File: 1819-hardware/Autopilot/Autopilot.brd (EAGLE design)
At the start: 44.8 x 54 mm, 36 parts, among them U1 MAX3485CSA, U3 PCA9306, U4 74HC1G04

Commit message: updated Autopilot board files
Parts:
- removed B2: Pressure Sensor, SparkFun-Boards:SPARKFUN_MS5803-14BA_BREAKOUT
- added J6: (no value), SparkFun-Connectors:1X07_NO_SILK
- moved R14 35.6 mm to (34.3, 22.2), flipped to the bottom
- moved C5 31.6 mm to (33.0, 39.4), turned to 180 degrees
- moved R15 29.6 mm to (30.5, 22.2), flipped to the bottom
- moved U3 5.24 mm to (27.9, 40.0), flipped to the bottom
- moved U$1 5.12 mm to (5.71, 14.6)
- moved R13 3.81 mm to (33.0, 41.3), flipped to the bottom, turned to 180 degrees
- moved U4 3.81 mm to (8.89, 33.7)
- moved C6 2.62 mm to (2.54, 7.62), flipped to the bottom
- moved J3 2.54 mm to (19.1, 2.54), turned to 180 degrees
- moved U1 2.29 mm to (8.89, 25.4)
- moved C2 2.01 mm to (6.99, 7.62), flipped to the bottom, turned to 180 degrees
- moved C1 1.27 mm to (27.3, 16.5)
- moved R10 1.27 mm to (10.2, 17.8), turned to 180 degrees
- moved R11 1.27 mm to (10.2, 14.0), turned to 180 degrees
- moved R12 1.27 mm to (10.2, 15.9), turned to 180 degrees
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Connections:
- removed net RESET: B1.13, B1.3
- net 3V3: now also J6.2; no longer B2.3.3V
- net BLUE: now also B1.14; no longer B1.16
- net GND: now also J6.1; no longer B2.GND
- net N$19: now also C5.1
- net RED: now also B1.16; no longer B1.14
- net SCL3V3: now also J6.4; no longer B2.SCL/SCLK
- net SDA3V3: now also J6.3; no longer B2.SDA/SDI
- net VCC: no longer C5.1
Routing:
- net SCL: track 0.00 -> 55.4 mm, vias 0 -> 3
- net SDA: track 0.00 -> 51.7 mm, vias 0 -> 1
- net VCC: track 0.00 -> 35.5 mm, vias 0 -> 13
- net 3V3: track 0.00 -> 31.1 mm, vias 0 -> 1
- net VOLTAGE_SENSOR: track 0.00 -> 31.0 mm, vias 0 -> 2
- net 485A: track 0.00 -> 27.9 mm
- net TX: track 0.00 -> 27.5 mm
- net 485B: track 0.00 -> 24.9 mm
- net RX: track 0.00 -> 20.4 mm
- net SDA-: track 0.00 -> 15.5 mm
- net SCL-: track 0.00 -> 14.8 mm
- net RED: track 0.00 -> 13.6 mm
- net SDA+: track 0.00 -> 13.6 mm
- net SCL+: track 0.00 -> 13.4 mm
- net GREEN: track 0.00 -> 13.3 mm
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- added copper zone on layer 16, net GND
- added copper zone on layer 1, net VCC
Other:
- board size 44.8 x 54 mm -> 44.4 x 54 mm

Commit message: started motorcontroller board files
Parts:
- J5: device SparkFun-Connectors:1X03 -> SparkFun-Connectors:1X03_LONGPADS
- R13, R16: value 100k -> 47k
- moved J5 0.90 mm to (2.54, 3.17)
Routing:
- net 12V: track 9.93 -> 9.04 mm
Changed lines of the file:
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@@
 <drawing>
 <settings>
-<setting alwaysvectorfont="yes"/>
+<setting alwaysvectorfont="no"/>
 <setting verticaltext="up"/>
 </settings>
@@
 <attribute name="PROD_ID" value="CONN-09696" x="28.575" y="2.54" size="1.778" layer="27" display="off"/>
 </element>
-<element name="J5" library="SparkFun-Connectors" library_urn="urn:adsk.eagle:library:513" package="1X03" package3d_urn="urn:adsk.eagle:package:38063/1" value="" x="3.175" y="2.54"/>
+<element name="J5" library="SparkFun-Connectors" package="1X03_LONGPADS" value="" x="2.54" y="3.175"/>
 <element name="R1" library="SparkFun-Resistors" library_urn="urn:adsk.eagle:library:532" package="0603" package3d_urn="urn:adsk.eagle:package:39650/1" value="100" x="17.78" y="5.715" rot="MR0">
 <attribute name="PROD_ID" value="RES-12438" x="17.78" y="5.715" size="1.778" layer="28" rot="MR0" display="off"/>
@@
 <attribute name="PROD_ID" value="RES-07861" x="10.16" y="15.875" size="1.778" layer="27" rot="R180" display="off"/>
 </element>
-<element name="R13" library="SparkFun-Resistors" library_urn="urn:adsk.eagle:library:532" package="0603" package3d_urn="urn:adsk.eagle:package:39650/1" value="100k" x="33.02" y="41.275" rot="MR180">
+<element name="R13" library="SparkFun-Resistors" library_urn="urn:adsk.eagle:library:532" package="0603" package3d_urn="urn:adsk.eagle:package:39650/1" value="47k" x="33.02" y="41.275" rot="MR180">
 <attribute name="PROD_ID" value="RES-07828" x="33.02" y="41.275" size="1.778" layer="28" rot="MR180" display="off"/>
 </element>
@@
 <attribute name="PROD_ID" value="RES-07857" x="30.48" y="22.225" size="1.778" layer="28" rot="MR180" display="off"/>
 </element>
-<element name="R16" library="SparkFun-Resistors" library_urn="urn:adsk.eagle:library:532" package="0603" package3d_urn="urn:adsk.eagle:package:39650/1" value="100k" x="12.065" y="5.715" rot="MR0">
+<element name="R16" library="SparkFun-Resistors" library_urn="urn:adsk.eagle:library:532" package="0603" package3d_urn="urn:adsk.eagle:package:39650/1" value="47k" x="12.065" y="5.715" rot="MR0">
 <attribute name="PROD_ID" value="RES-07828" x="12.065" y="5.715" size="1.778" layer="28" rot="MR0" display="off"/>
 </element>
@@
 <wire x1="3.4036" y1="11.5062" x2="3.4036" y2="7.6336" width="0.508" layer="16"/>
 <wire x1="3.4036" y1="7.6336" x2="3.39" y2="7.62" width="0.2032" layer="16"/>
-<wire x1="3.39" y1="7.62" x2="3.39" y2="4.865" width="0.508" layer="16"/>
-<wire x1="3.39" y1="4.865" x2="5.715" y2="2.54" width="0.508" layer="16"/>
+<wire x1="3.39" y1="7.62" x2="5.08" y2="5.93" width="0.508" layer="16"/>
+<wire x1="5.08" y1="5.93" x2="5.08" y2="3.175" width="0.508" layer="16"/>
 </signal>
 <signal name="TX">
@@
 <contactref element="J5" pad="3"/>
 <contactref element="R16" pad="2"/>
-<wire x1="8.255" y1="2.54" x2="11.215" y2="5.5" width="0.2032" layer="16"/>
-<wire x1="11.215" y1="5.5" x2="11.215" y2="5.715" width="0.2032" layer="16"/>
+<wire x1="7.62" y1="3.175" x2="10.16" y2="5.715" width="0.2032" layer="16"/>
+<wire x1="10.16" y1="5.715" x2="11.215" y2="5.715" width="0.2032" layer="16"/>
 </signal>
 </signals>

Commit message: worked on routing
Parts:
- FRAME1: value FRAME-LETTER -> FRAME-LETTERNO_PACKAGE; device SparkFun-Aesthetics:CREATIVE_COMMONS -> SparkFun-Aesthetics:DUMMY
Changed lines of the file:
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@@
 <layer number="14" name="Route14" color="1" fill="6" visible="no" active="no"/>
 <layer number="15" name="Route15" color="4" fill="6" visible="yes" active="yes"/>
-<layer number="16" name="Bottom" color="1" fill="1" visible="yes" active="yes"/>
+<layer number="16" name="Bottom" color="1" fill="1" visible="no" active="yes"/>
 <layer number="17" name="Pads" color="2" fill="1" visible="yes" active="yes"/>
 <layer number="18" name="Vias" color="2" fill="1" visible="yes" active="yes"/>
@@
 <layer number="20" name="Dimension" color="24" fill="1" visible="yes" active="yes"/>
 <layer number="21" name="tPlace" color="7" fill="1" visible="yes" active="yes"/>
-<layer number="22" name="bPlace" color="7" fill="1" visible="yes" active="yes"/>
-<layer number="23" name="tOrigins" color="15" fill="1" visible="yes" active="yes"/>
-<layer number="24" name="bOrigins" color="15" fill="1" visible="yes" active="yes"/>
+<layer number="22" name="bPlace" color="7" fill="1" visible="no" active="yes"/>
+<layer number="23" name="tOrigins" color="15" fill="1" visible="no" active="yes"/>
+<layer number="24" name="bOrigins" color="15" fill="1" visible="no" active="yes"/>
 <layer number="25" name="tNames" color="7" fill="1" visible="no" active="yes"/>
 <layer number="26" name="bNames" color="7" fill="1" visible="no" active="yes"/>
@@
 <attribute name="PROD_ID" value="CAP-00810" x="2.54" y="7.62" size="1.778" layer="28" rot="MR0" display="off"/>
 </element>
-<element name="FRAME1" library="SparkFun-Aesthetics" package="CREATIVE_COMMONS" value="FRAME-LETTER" x="26.67" y="-11.43"/>
+<element name="FRAME1" library="SparkFun-Aesthetics" package="DUMMY" value="FRAME-LETTERNO_PACKAGE" x="26.67" y="-11.43">
+<attribute name="DESIGNER" value="Nobody" x="26.67" y="-11.43" size="1.778" layer="27" display="off"/>
+<attribute name="VERSION" value="v01" x="26.67" y="-11.43" size="1.778" layer="27" display="off"/>
+</element>
 <element name="J1" library="SparkFun-Connectors" library_urn="urn:adsk.eagle:library:513" package="1X04_NO_SILK" package3d_urn="urn:adsk.eagle:package:38094/1" value="" x="41.91" y="20.955" rot="R270">
 <attribute name="PROD_ID" value="CONN-09696" x="41.91" y="20.955" size="1.778" layer="27" rot="R270" display="off"/>

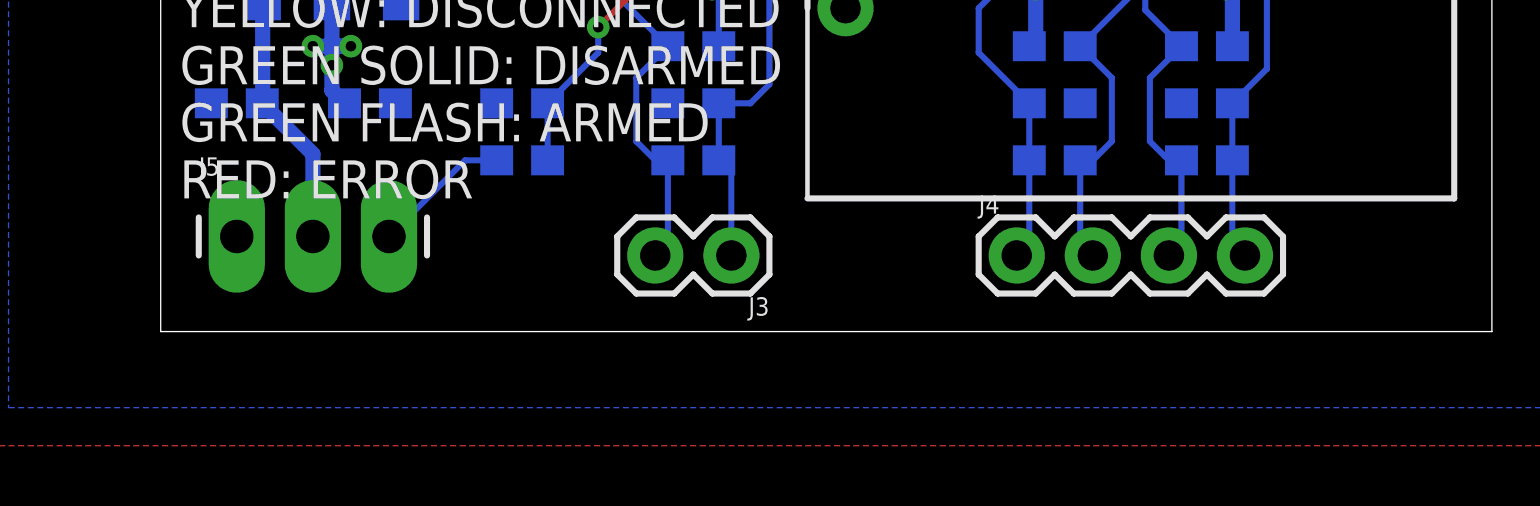
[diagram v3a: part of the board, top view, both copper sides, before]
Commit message: the arduino was upside down
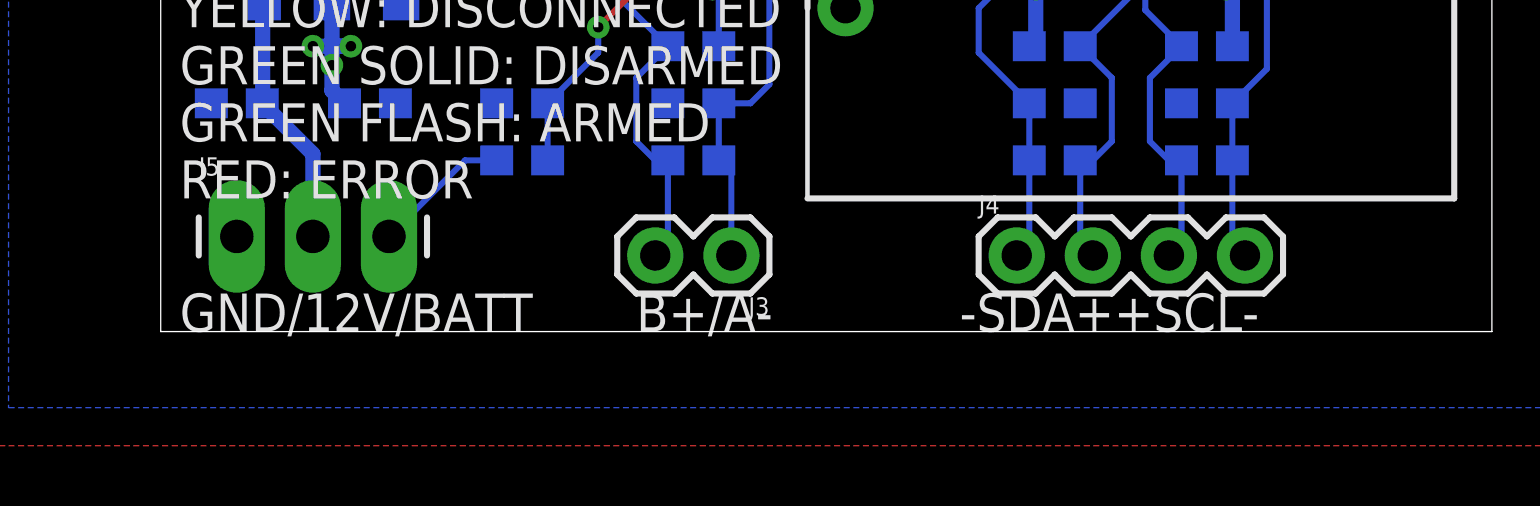
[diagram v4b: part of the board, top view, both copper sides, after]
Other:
- board text added: "-SDA++SCL-"
- board text added: "B+/A-"
- board text added: "GND/12V/BATT"
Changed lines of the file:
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@@
 <layer number="14" name="Route14" color="1" fill="6" visible="no" active="no"/>
 <layer number="15" name="Route15" color="4" fill="6" visible="yes" active="yes"/>
-<layer number="16" name="Bottom" color="1" fill="1" visible="no" active="yes"/>
+<layer number="16" name="Bottom" color="1" fill="1" visible="yes" active="yes"/>
 <layer number="17" name="Pads" color="2" fill="1" visible="yes" active="yes"/>
 <layer number="18" name="Vias" color="2" fill="1" visible="yes" active="yes"/>
@@
 <layer number="20" name="Dimension" color="24" fill="1" visible="yes" active="yes"/>
 <layer number="21" name="tPlace" color="7" fill="1" visible="yes" active="yes"/>
-<layer number="22" name="bPlace" color="7" fill="1" visible="no" active="yes"/>
+<layer number="22" name="bPlace" color="7" fill="1" visible="yes" active="yes"/>
 <layer number="23" name="tOrigins" color="15" fill="1" visible="no" active="yes"/>
 <layer number="24" name="bOrigins" color="15" fill="1" visible="no" active="yes"/>
@@
 </layers>
 <board>
+<fusionsync huburn="a.cGVyc29uYWw6dWUyYjgwY2M1" projecturn="a.cGVyc29uYWw6dWUyODFhMmJiIzIwMTcxMjEwMTA3ODgzOTA2" f3durn="urn:adsk.wipprod:dm.lineage:uD4Zcr9FTMO__W5u9QbE6w" pcbguid="134edd82-9e4b-4083-93db-28e6e479e9f3" lastpulledtime="" lastsyncedchangeguid="1afef2b7-b8c7-2421-b492-ca9f02f62a60"/>
 <plain>
 <wire x1="0" y1="0" x2="44.4375" y2="0" width="0" layer="20"/>
@@
 <wire x1="40.005" y1="52.07" x2="21.59" y2="52.07" width="0.2032" layer="21"/>
 <wire x1="21.59" y1="52.07" x2="21.59" y2="31.75" width="0.2032" layer="21"/>
+<text x="26.67" y="0" size="1.27" layer="21" font="vector">-SDA++SCL-</text>
+<text x="15.875" y="0" size="1.27" layer="21" font="vector">B+/A-</text>
+<text x="0.635" y="0" size="1.27" layer="21" font="vector">GND/12V/BATT</text>
 </plain>
 <attributes>
@@
 </note>
 <note version="8.3" severity="warning">
+Since Version 8.3, EAGLE supports Fusion synchronisation.
+This feature will not be available in this version and saving
+the document will break the link to the Fusion PCB feature.
+</note>
+<note version="8.3" severity="warning">

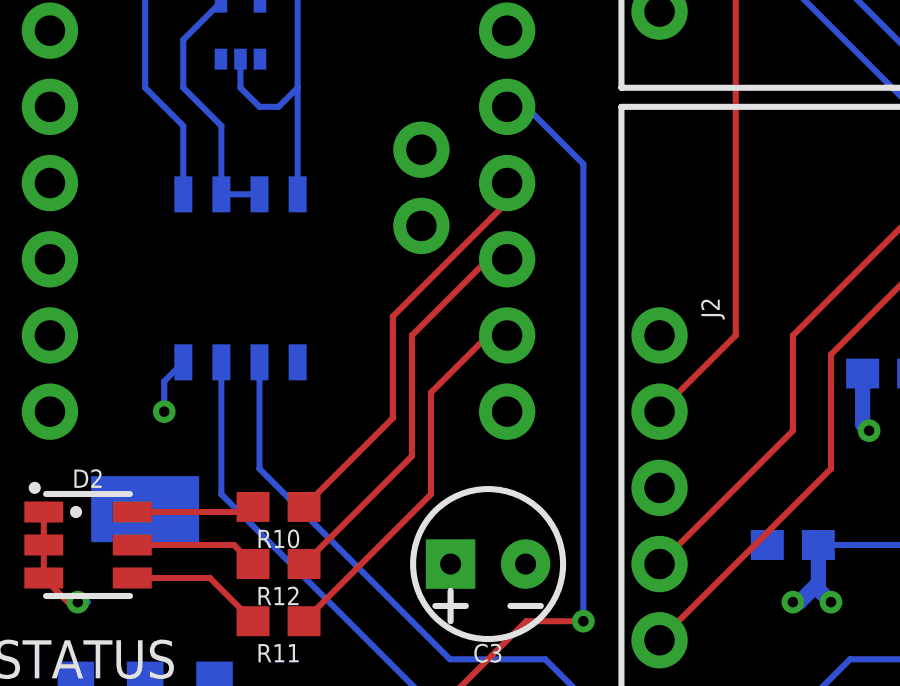
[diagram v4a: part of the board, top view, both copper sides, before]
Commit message: pindefs in firmware match board files
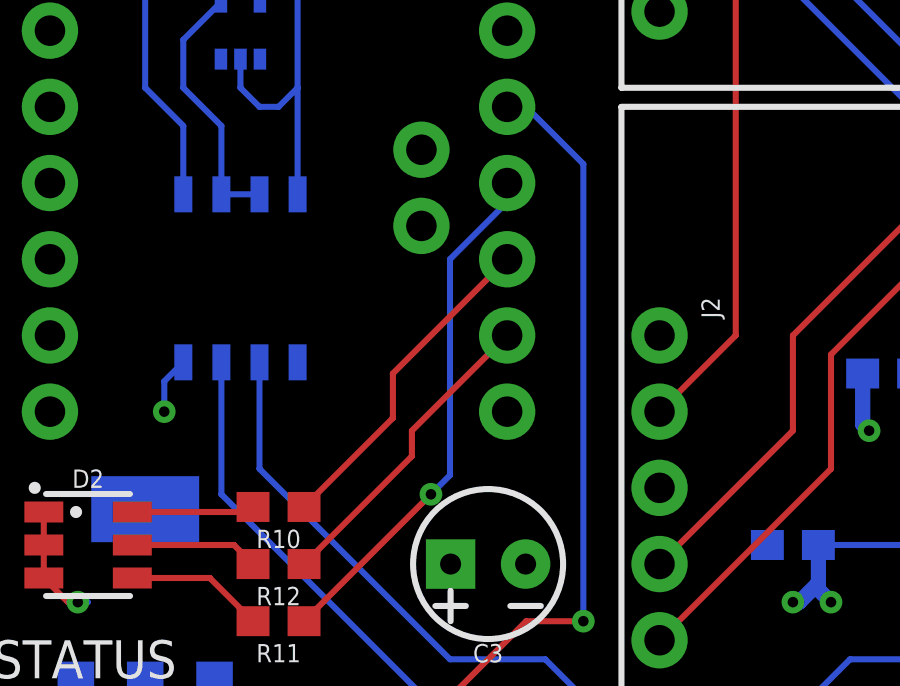
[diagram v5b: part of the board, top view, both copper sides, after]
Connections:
- net BLUE: now also B1.16; no longer B1.14
- net GREEN: now also B1.14; no longer B1.15
- net RED: now also B1.15; no longer B1.16
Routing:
- net BLUE: track 12.7 -> 17.4 mm, vias 0 -> 1
- net GREEN: track 13.3 -> 10.4 mm
- net RED: track 13.6 -> 11.1 mm
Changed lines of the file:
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@@
 <signal name="RED">
 <contactref element="R10" pad="1"/>
-<contactref element="B1" pad="16"/>
 <wire x1="11.01" y1="17.78" x2="13.97" y2="20.74" width="0.2032" layer="1"/>
-<wire x1="13.97" y1="20.74" x2="13.97" y2="24.13" width="0.2032" layer="1"/>
-<wire x1="13.97" y1="24.13" x2="17.78" y2="27.94" width="0.2032" layer="1"/>
-<wire x1="17.78" y1="27.94" x2="17.78" y2="28.575" width="0.2032" layer="1"/>
+<contactref element="B1" pad="15"/>
+<wire x1="13.97" y1="20.74" x2="13.97" y2="22.225" width="0.2032" layer="1"/>
+<wire x1="13.97" y1="22.225" x2="17.78" y2="26.035" width="0.2032" layer="1"/>
 </signal>
 <signal name="GREEN">
-<contactref element="B1" pad="15"/>
 <contactref element="R12" pad="1"/>
 <wire x1="11.01" y1="15.875" x2="14.605" y2="19.47" width="0.2032" layer="1"/>
-<wire x1="14.605" y1="19.47" x2="14.605" y2="23.495" width="0.2032" layer="1"/>
-<wire x1="14.605" y1="23.495" x2="17.145" y2="26.035" width="0.2032" layer="1"/>
-<wire x1="17.145" y1="26.035" x2="17.78" y2="26.035" width="0.2032" layer="1"/>
+<contactref element="B1" pad="14"/>
+<wire x1="14.605" y1="19.47" x2="14.605" y2="20.32" width="0.2032" layer="1"/>
+<wire x1="14.605" y1="20.32" x2="17.78" y2="23.495" width="0.2032" layer="1"/>
 </signal>
 <signal name="BLUE">
 <contactref element="R11" pad="1"/>
-<contactref element="B1" pad="14"/>
 <wire x1="11.01" y1="13.97" x2="15.24" y2="18.2" width="0.2032" layer="1"/>
-<wire x1="15.24" y1="18.2" x2="15.24" y2="21.59" width="0.2032" layer="1"/>
-<wire x1="15.24" y1="21.59" x2="17.145" y2="23.495" width="0.2032" layer="1"/>
-<wire x1="17.145" y1="23.495" x2="17.78" y2="23.495" width="0.2032" layer="1"/>
+<contactref element="B1" pad="16"/>
+<via x="15.24" y="18.2" extent="1-16" drill="0.35"/>
+<wire x1="15.24" y1="18.2" x2="15.875" y2="18.835" width="0.2032" layer="16"/>
+<wire x1="17.78" y1="27.94" x2="17.78" y2="28.575" width="0.2032" layer="16"/>
+<wire x1="15.875" y1="18.835" x2="15.875" y2="26.035" width="0.2032" layer="16"/>
+<wire x1="15.875" y1="26.035" x2="17.78" y2="27.94" width="0.2032" layer="16"/>
 </signal>
 <signal name="SDA">
